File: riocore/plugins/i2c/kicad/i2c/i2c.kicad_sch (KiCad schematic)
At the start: 8 parts, among them U2 ISO1540

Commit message: i2c: kicad: fixes
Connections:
- net 3v3 renamed +3.3V
- net SCL renamed scl
- net SDA renamed sda
- net gnd renamed GND

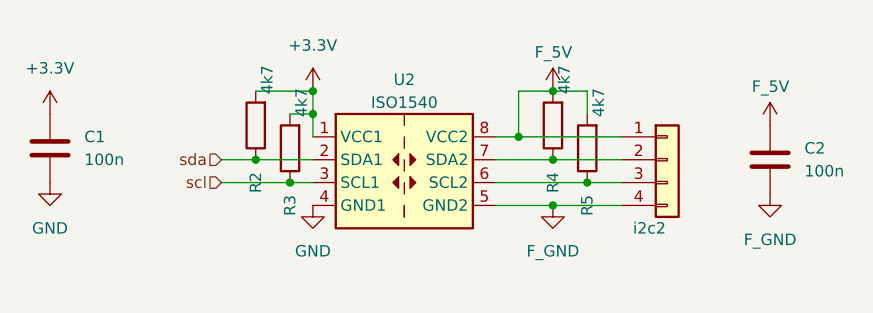
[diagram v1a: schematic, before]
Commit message: kicad: get power-signals
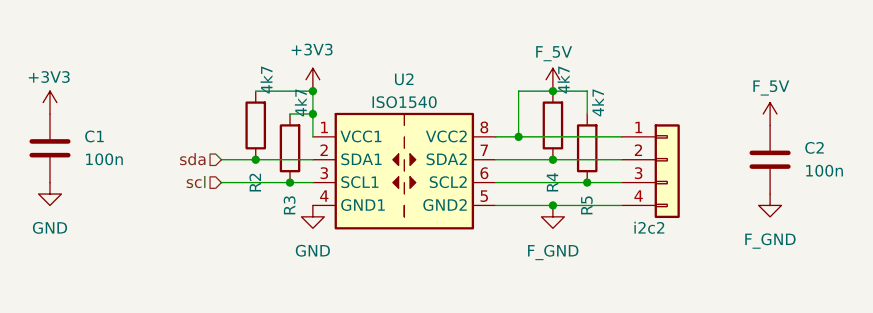
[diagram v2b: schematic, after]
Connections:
- net +3.3V renamed +3V3
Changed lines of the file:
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@@
 		(on_board yes)
 		(dnp no)
-		(fields_autoplaced yes)
 		(property "Reference" "#PWR03"
 			(at 125.73 87.63 0)
@@
 			)
 		)
-		(property "Value" "+3.3V"
-			(at 125.73 78.74 0)
-			(effects
-				(font
-					(size 1.27 1.27)
-				)
+		(property "Value" "+3V3"
+			(at 123.19 79.248 0)
+			(effects
+				(font
+					(size 1.27 1.27)
+				)
+				(justify left)
 			)
 		)
@@
 		(on_board yes)
 		(dnp no)
-		(fields_autoplaced yes)
 		(property "Reference" "#PWR05"
 			(at 96.52 90.17 0)
@@
 			)
 		)
-		(property "Value" "+3.3V"
-			(at 96.52 81.28 0)
-			(effects
-				(font
-					(size 1.27 1.27)
-				)
-			)
-		)
+		(property "Value" "+3V3"
+			(at 93.98 82.296 0)
+			(effects
+				(font
+					(size 1.27 1.27)
+				)
+				(justify left)
+			)
+		)
